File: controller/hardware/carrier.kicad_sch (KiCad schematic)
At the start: 48 parts, among them J1 6P6C, J10 WIZ850io J1 (SPI), J11 WIZ850io J2 (power, reset), J2 6P6C, J3 6P6C, J4 6P6C, J5 8P8C, J6 Panel DC in, 2.1 mm, U1 THVD1410, U2 THVD1410, U3 THVD1410, U4 THVD1410, U5 THVD1410

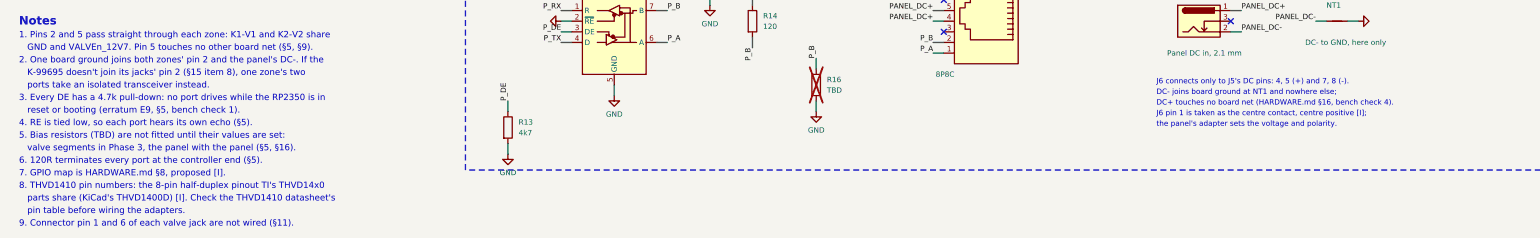
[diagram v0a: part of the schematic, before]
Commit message: Lay out the carrier PCB from the schematic's script
The protoboard carrier becomes a two-layer board, 160 x 60 mm, shaped to the
Hammond 1591ESBK: every jack mouth and the Pico 2's USB socket on the edge
against the wall the cables come through, a notch for that wall's middle lid
boss, four M2.5 holes. carrier_board.py places the parts from the netlist,
replays Freerouting's routing from carrier.ses, pours ground on both layers
and runs KiCad's DRC, which finds nothing. Nobody edits it in KiCad.

The schematic now names each part's footprint and part number. The valve
jacks change from the Wurth 615006138421 to the Amphenol 54601-906LF: KiCad's
footprint for the Amphenol is drawn from Amphenol's drawing, and no Wurth
drawing could be fetched. The Pico 2 and WIZ850io footprints are the project's
own (carrier_footprints.py), from the Pico 2 datasheet and WIZnet's drawing.
Before, the schematic carried no footprints and the board didn't exist.

UUIDs are seeded, so a rebuild with KiCad 7.0.11 writes the same bytes.

Co-Authored-By: Claude Opus 5.5 (1M context) <noreply@anthropic.com>
Claude-Session: https://claude.ai/code/session_01PNaoTTizvWnVxnC9Mh2V5e
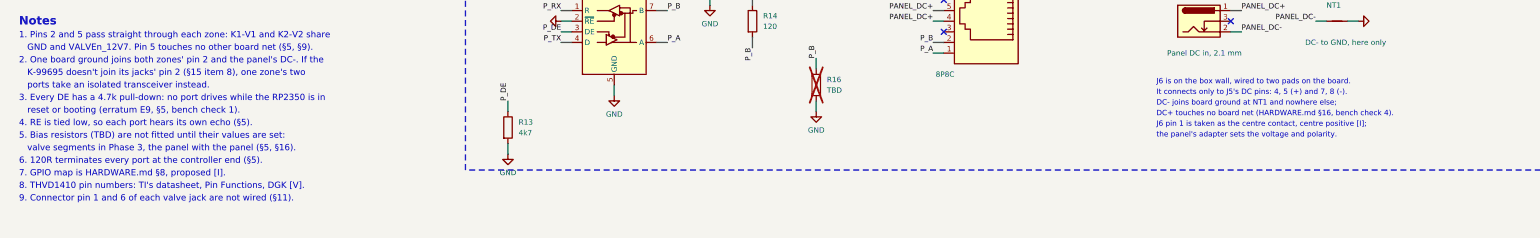
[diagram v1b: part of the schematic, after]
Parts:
- A1: footprint (none) -> carrier:Pico2_Socketed; Manufacturer (none) -> Raspberry Pi; Socket (none) -> 2 x 1x20 female header, Sullins PPPC201LFBN-RC (DigiKey S70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
- C1, C2, C3, C4, C5: footprint (none) -> Capacitor_THT:C_Rect_L4.0mm_W2.5mm_P2.50mm; MPN (none) -> K104K15X7RF5TL2; Manufacturer (none) -> Vishay; Supplier (none) -> DigiKey BC1084CT-ND
- J1, J2, J3, J4: footprint (none) -> Connector_RJ:RJ12_Amphenol_54601-x06_Horizontal; MPN 615006138421 -> 54601-906LF; Manufacturer Würth Elektronik -> Amphenol ICC; Supplier DigiKey 732-2113-ND -> DigiKey, product 7589414
- J10: footprint (none) -> carrier:WIZ850io_J1; Manufacturer (none) -> WIZnet; Socket (none) -> 1x6 female header, 2.54 mm, cut from a PPPC201LFBN-RC
- J11: footprint (none) -> carrier:WIZ850io_J2; Socket (none) -> 1x6 female header, 2.54 mm, cut from a PPPC201LFBN-RC
- J5: footprint (none) -> Connector_RJ:RJ45_Amphenol_54602-x08_Horizontal; Manufacturer Amphenol -> Amphenol ICC
- J6: footprint (none) -> Connector_Wire:SolderWire-0.5sqmm_1x02_P4.8mm_D0.9mm_OD2.3mm; Mounting (none) -> Box wall; two wires to the board's J6 pads
- NT1: footprint (none) -> NetTie:NetTie-2_SMD_Pad0.5mm
- R1, R13, R3, R7, R9: footprint (none) -> Resistor_THT:R_Axial_DIN0207_L6.3mm_D2.5mm_P10.16mm_Horizontal; MPN (none) -> CFR-25JB-52-4K7; Manufacturer (none) -> Yageo; Supplier (none) -> DigiKey 13-CFR-25JB-52-4K7-ND
- R10, R14, R2, R4, R8: footprint (none) -> Resistor_THT:R_Axial_DIN0207_L6.3mm_D2.5mm_P10.16mm_Horizontal; MPN (none) -> CFR-25JB-52-120R; Manufacturer (none) -> Yageo; Supplier (none) -> DigiKey 120QBK-ND
- R11, R12, R15, R16, R5, R6: footprint (none) -> Resistor_THT:R_Axial_DIN0207_L6.3mm_D2.5mm_P10.16mm_Horizontal
- TP1, TP10, TP11, TP12, TP2, TP3, TP4, TP5, TP6, TP7, TP8, TP9: footprint (none) -> Connector_PinHeader_2.54mm:PinHeader_1x01_P2.54mm_Vertical; MPN (none) -> 1x1 male header, 2.54 mm; Supplier (none) -> Already owned
- U1, U2, U3, U4, U5: footprint (none) -> Package_SO:VSSOP-8_3.0x3.0mm_P0.65mm; Manufacturer (none) -> Texas Instruments
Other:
- note added: "8. THVD1410 pin numbers: TI's datasheet, Pin Functions, DGK [V]."
- note added: "It connects only to J5's DC pins: 4, 5 (+) and 7, 8 (-)."
- note added: "J6 is on the box wall, wired to two pads on the board."
- note removed: "8. THVD1410 pin numbers: the 8-pin half-duplex pinout TI's THVD14x0"
- note removed: "J6 connects only to J5's DC pins: 4, 5 (+) and 7, 8 (-)."
- note removed: "parts share (KiCad's THVD1400D) [I]. Check the THVD1410 datasheet's"
- note removed: "pin table before wiring the adapters."

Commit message: Carrier PCB: valve jacks back to the Würth 615006138421
The board's four valve jacks were the Amphenol 54601-906LF, picked this
morning because KiCad has a footprint for it. Mouser lists it obsolete
(discontinuance notice 2024-01-15), so the board goes back to the Würth
615006138421 already in the order.

Its footprint is new, written by carrier_footprints.py from Würth's data
sheet, rev 001.001: six 0.9 mm holes at 1.02 mm pitch in two rows 2.54 mm
apart, two 2.36 mm unplated pegs 12 mm apart. The mouth is taken as the peg
side, 6 mm ahead of the pegs, read from the drawings rather than measured.
The jack rows move so each mouth stays on the board edge; the port columns
don't change. Rerouted: 0 DRC violations, 0 unconnected, and a second run
reproduces every file byte for byte.

The shopping list drops what the corrected cart dropped (the 2x6 socket,
the Adafruit adapters, the Perma-Proto), records that the order hasn't been
placed, notes the Mouser lifecycle check of every board part, and marks the
PCB ready to order.

Co-Authored-By: Claude Opus 5.5 (1M context) <noreply@anthropic.com>
Claude-Session: https://claude.ai/code/session_01PNaoTTizvWnVxnC9Mh2V5e
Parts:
- J1, J2, J3, J4: footprint Connector_RJ:RJ12_Amphenol_54601-x06_Horizontal -> carrier:RJ12_Wurth_615006138421_Horizontal; MPN 54601-906LF -> 615006138421; Manufacturer Amphenol ICC -> Würth Elektronik; Supplier DigiKey, product 7589414 -> DigiKey 732-2113-ND
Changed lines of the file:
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@@
     (property
       "Footprint"
-      "Connector_RJ:RJ12_Amphenol_54601-x06_Horizontal"
+      "carrier:RJ12_Wurth_615006138421_Horizontal"
       (at 246.38 43.18 0)
       (effects (font (size 1.27 1.27)) hide))
@@
     (property
       "MPN"
-      "54601-906LF"
+      "615006138421"
       (at 246.38 43.18 0)
       (effects (font (size 1.27 1.27)) hide))
     (property
       "Manufacturer"
-      "Amphenol ICC"
+      "Würth Elektronik"
       (at 246.38 43.18 0)
       (effects (font (size 1.27 1.27)) hide))
     (property
       "Supplier"
-      "DigiKey, product 7589414"
+      "DigiKey 732-2113-ND"
       (at 246.38 43.18 0)
       (effects (font (size 1.27 1.27)) hide))
@@
     (property
       "Footprint"
-      "Connector_RJ:RJ12_Amphenol_54601-x06_Horizontal"
+      "carrier:RJ12_Wurth_615006138421_Horizontal"
       (at 391.16 43.18 0)
       (effects (font (size 1.27 1.27)) hide))
@@
     (property
       "MPN"
-      "54601-906LF"
+      "615006138421"
       (at 391.16 43.18 0)
       (effects (font (size 1.27 1.27)) hide))
     (property
       "Manufacturer"
-      "Amphenol ICC"
+      "Würth Elektronik"
       (at 391.16 43.18 0)
       (effects (font (size 1.27 1.27)) hide))
     (property
       "Supplier"
-      "DigiKey, product 7589414"
+      "DigiKey 732-2113-ND"
       (at 391.16 43.18 0)
       (effects (font (size 1.27 1.27)) hide))
@@
     (property
       "Footprint"
-      "Connector_RJ:RJ12_Amphenol_54601-x06_Horizontal"
+      "carrier:RJ12_Wurth_615006138421_Horizontal"
       (at 246.38 114.3 0)
       (effects (font (size 1.27 1.27)) hide))
@@
     (property
       "MPN"
-      "54601-906LF"
+      "615006138421"
       (at 246.38 114.3 0)
       (effects (font (size 1.27 1.27)) hide))
     (property
       "Manufacturer"
-      "Amphenol ICC"
+      "Würth Elektronik"
       (at 246.38 114.3 0)
       (effects (font (size 1.27 1.27)) hide))
     (property
       "Supplier"
-      "DigiKey, product 7589414"
+      "DigiKey 732-2113-ND"
       (at 246.38 114.3 0)
       (effects (font (size 1.27 1.27)) hide))
@@
     (property
       "Footprint"
-      "Connector_RJ:RJ12_Amphenol_54601-x06_Horizontal"
+      "carrier:RJ12_Wurth_615006138421_Horizontal"
       (at 391.16 114.3 0)
       (effects (font (size 1.27 1.27)) hide))
@@
     (property
       "MPN"
-      "54601-906LF"
+      "615006138421"
       (at 391.16 114.3 0)
       (effects (font (size 1.27 1.27)) hide))
     (property
       "Manufacturer"
-      "Amphenol ICC"
+      "Würth Elektronik"
       (at 391.16 114.3 0)
       (effects (font (size 1.27 1.27)) hide))
     (property
       "Supplier"
-      "DigiKey, product 7589414"
+      "DigiKey 732-2113-ND"
       (at 391.16 114.3 0)
       (effects (font (size 1.27 1.27)) hide))
